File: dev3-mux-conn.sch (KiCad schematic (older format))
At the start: 9 parts, among them J27 Device 3, U16 TS12A44514, U17 TS12A44514, U20 MAX4533, U57 74LS32, U58 LTC1391, U59 LTC1391, U60 LTC1391

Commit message: Updating power + libraries
- Reannotated all parts
- Migrated to new OR gate library
- Reorganized power sheet
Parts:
- removed U57: 74LS32, SMD_Packages:SSOP-14, symbol 74LS32
- added U14: 74LS32, symbol 74LS32
- renumbered C245 to C53, J27 to J29, U20 to U11, U58 to U39, U59 to U40, U60 to U41, U17 to U7, U16 to U7
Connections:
- wire segments 76 -> 77
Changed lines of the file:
@@
-EESchema Schematic File Version 2
+EESchema Schematic File Version 3
 LIBS:SW-Texas
 LIBS:power
@@
 $Descr USLetter 11000 8500
 encoding utf-8
-Sheet 7 15
+Sheet 8 15
 Title ""
 Date ""
@@
 $EndDescr
 $Comp
-L Conn_01x07 J27
+L Conn_01x07 J29
 U 1 1 58EAAC27
 P 850 1200
-F 0 "J27" H 850 1650 50  0000 C CNN
+F 0 "J29" H 850 1650 50  0000 C CNN
 F 1 "Device 3" V 950 1200 50  0000 C CNN
 F 2 "Pin_Headers:Pin_Header_Straight_1x07_Pitch2.54mm" H 850 1200 50  0001 C CNN
@@
 AR Path="/58DEDA38/58EAAC33" Ref="U?"  Part="1"
 AR Path="/58DEDA38/58E9E25B/58EAAC33" Ref="U?"  Part="1"
-AR Path="/58DEDA38/58E9E9F4/58EAAC33" Ref="U17"  Part="4"
-F 0 "U17" H 2650 1450 60  0000 C CNN
+AR Path="/58DEDA38/58E9E9F4/58EAAC33" Ref="U7"  Part="4"
+F 0 "U7" H 2650 1450 60  0000 C CNN
 F 1 "TS12A44514" H 3300 1400 60  0000 C CNN
 F 2 "Housings_SSOP:TSSOP-14_4.4x5mm_Pitch0.65mm" H 3400 2500 60  0001 C CNN
@@
 $Comp
 L TS12A44514 U?
-U 4 1 58EAAC3F
+U 3 1 58EAAC3F
 P 1650 1500
 AR Path="/58DEDA38/58EAAC3F" Ref="U?"  Part="1"
 AR Path="/58DEDA38/58E9E25B/58EAAC3F" Ref="U?"  Part="1"
-AR Path="/58DEDA38/58E9E9F4/58EAAC3F" Ref="U16"  Part="4"
-F 0 "U16" H 1350 1450 60  0000 C CNN
+AR Path="/58DEDA38/58E9E9F4/58EAAC3F" Ref="U7"  Part="3"
+F 0 "U7" H 1350 1450 60  0000 C CNN
 F 1 "TS12A44514" H 1350 1350 60  0000 C CNN
 F 2 "Housings_SSOP:TSSOP-14_4.4x5mm_Pitch0.65mm" H 2150 2800 60  0001 C CNN
@@
 F 7 "TSSOP14" H 1950 2700 60  0001 C CNN "Package ID"
 F 8 "0.00@0" H 1700 2500 60  0001 C CNN "Pricing"
-	4    1650 1500
-	1    0    0    -1
-$EndComp
-$Comp
-L C_Small C245
+	3    1650 1500
+	1    0    0    -1
+$EndComp
+$Comp
+L C_Small C53
 U 1 1 58EAAC46
 P 2450 1200
-F 0 "C245" H 2460 1270 50  0000 L CNN
+F 0 "C53" H 2460 1270 50  0000 L CNN
 F 1 "10u" H 2460 1120 50  0000 L CNN
 F 2 "Capacitors_SMD:C_0603" H 2450 1200 50  0001 C CNN
@@
 AUDIO-GROUND
 $Comp
-L LTC1391 U58
+L LTC1391 U39
 U 1 1 58EAAC56
 P 6350 1450
-F 0 "U58" H 6100 1950 60  0000 C CNN
+F 0 "U39" H 6100 1950 60  0000 C CNN
 F 1 "LTC1391" H 6700 1900 60  0000 C CNN
 F 2 "Housings_SSOP:SSOP-16_3.9x4.9mm_Pitch0.635mm" H 6450 2700 60  0001 C CNN
@@
 DOUT
 $Comp
-L +5VD #PWR0211
+L +5VD #PWR078
 U 1 1 58EAAC61
 P 6350 750
-F 0 "#PWR0211" H 6350 600 50  0001 C CNN
+F 0 "#PWR078" H 6350 600 50  0001 C CNN
 F 1 "+5VD" H 6350 890 50  0000 C CNN
 F 2 "" H 6350 750 50  0001 C CNN
@@
 $EndComp
 $Comp
-L GNDREF #PWR0212
+L GNDREF #PWR079
 U 1 1 58EAAC67
 P 6350 2050
-F 0 "#PWR0212" H 6350 1800 50  0001 C CNN
+F 0 "#PWR079" H 6350 1800 50  0001 C CNN
 F 1 "GNDREF" H 6350 1900 50  0000 C CNN
 F 2 "" H 6350 2050 50  0001 C CNN
@@
 Text HLabel 7100 1800 2    60   Input ~ 0
 MIC-IN-7
-$Comp
-L 74LS32 U57
-U 1 1 58EAAC75
-P 3450 2900
-F 0 "U57" H 3450 2950 50  0000 C CNN
-F 1 "74LS32" H 3450 2850 50  0000 C CNN
-F 2 "SMD_Packages:SSOP-14" H 3450 2900 50  0001 C CNN
-F 3 "" H 3450 2900 50  0001 C CNN
-F 4 "0.00@0" H 3450 2900 60  0001 C CNN "Pricing"
-	1    3450 2900
-	-1   0    0    1
-$EndComp
-$Comp
-L 74LS32 U57
-U 2 1 58EAAC7C
-P 3450 4600
-F 0 "U57" H 3450 4650 50  0000 C CNN
-F 1 "74LS32" H 3450 4550 50  0000 C CNN
-F 2 "SMD_Packages:SSOP-14" H 3450 4600 50  0001 C CNN
-F 3 "" H 3450 4600 50  0001 C CNN
-F 4 "0.00@0" H 3450 4600 60  0001 C CNN "Pricing"
-	2    3450 4600
-	-1   0    0    1
-$EndComp
 Text HLabel 4250 2800 2    60   Input ~ 0
 MIC-MUTE-Pi
@@
 P 2300 1650
 AR Path="/58DEDA38/58E9E25B/58EAAC89" Ref="U?"  Part="1"
-AR Path="/58DEDA38/58E9E9F4/58EAAC89" Ref="U20"  Part="4"
-F 0 "U20" H 2400 1850 60  0000 C CNN
+AR Path="/58DEDA38/58E9E9F4/58EAAC89" Ref="U11"  Part="4"
+F 0 "U11" H 2400 1850 60  0000 C CNN
 F 1 "MAX4533" H 1950 1400 60  0000 C CNN
 F 2 "Housings_SSOP:SSOP-20_4.4x6.5mm_Pitch0.65mm" H 2400 2600 60  0001 C CNN
@@
 PTT-7
 $Comp
-L LTC1391 U59
+L LTC1391 U40
 U 1 1 58EAACA4
 P 6350 3250
-F 0 "U59" H 6100 3750 60  0000 C CNN
+F 0 "U40" H 6100 3750 60  0000 C CNN
 F 1 "LTC1391" H 6700 3700 60  0000 C CNN
 F 2 "Housings_SSOP:SSOP-16_3.9x4.9mm_Pitch0.635mm" H 6450 4500 60  0001 C CNN
@@
 $EndComp
 $Comp
-L +5VD #PWR0213
+L +5VD #PWR080
 U 1 1 58EAACAB
 P 6350 2550
-F 0 "#PWR0213" H 6350 2400 50  0001 C CNN
+F 0 "#PWR080" H 6350 2400 50  0001 C CNN
 F 1 "+5VD" H 6350 2690 50  0000 C CNN
 F 2 "" H 6350 2550 50  0001 C CNN
@@
 $EndComp
 $Comp
-L GNDREF #PWR0214
+L GNDREF #PWR081
 U 1 1 58EAACB1
 P 6350 3850
-F 0 "#PWR0214" H 6350 3600 50  0001 C CNN
+F 0 "#PWR081" H 6350 3600 50  0001 C CNN
 F 1 "GNDREF" H 6350 3700 50  0000 C CNN
 F 2 "" H 6350 3850 50  0001 C CNN
@@
 $EndComp
 $Comp
-L LTC1391 U60
+L LTC1391 U41
 U 1 1 58EAACBB
 P 6350 4950
-F 0 "U60" H 6100 5450 60  0000 C CNN
+F 0 "U41" H 6100 5450 60  0000 C CNN
 F 1 "LTC1391" H 6700 5400 60  0000 C CNN
 F 2 "Housings_SSOP:SSOP-16_3.9x4.9mm_Pitch0.635mm" H 6450 6200 60  0001 C CNN
@@
 $EndComp
 $Comp
-L +5VD #PWR0215
+L +5VD #PWR082
 U 1 1 58EAACC2
 P 6350 4250
-F 0 "#PWR0215" H 6350 4100 50  0001 C CNN
+F 0 "#PWR082" H 6350 4100 50  0001 C CNN
 F 1 "+5VD" H 6350 4390 50  0000 C CNN
 F 2 "" H 6350 4250 50  0001 C CNN
@@
 $EndComp
 $Comp
-L GNDREF #PWR0216
+L GNDREF #PWR083
 U 1 1 58EAACC8
 P 6350 5550
-F 0 "#PWR0216" H 6350 5300 50  0001 C CNN
+F 0 "#PWR083" H 6350 5300 50  0001 C CNN
 F 1 "GNDREF" H 6350 5400 50  0000 C CNN
 F 2 "" H 6350 5550 50  0001 C CNN
@@
 Connection ~ 3300 1550
 Wire Wire Line
-	2850 4600 2650 4600
+	2650 4600 3450 4600
 Wire Wire Line
 	2650 4600 2650 1750
@@
 Text Notes 1450 3000 0    60   ~ 0
 1-Audio Ground\n2-L audio to MUX\n3-R audio to MUX\n4-Mic +\n5-Mic -\n6- PTT +\n7- PTT -
+$Comp
+L 74LS32 U?
+U 3 1 59D24359
+P 3750 2900
+AR Path="/58DEDA38/58E9E2BE/59D24359" Ref="U?"  Part="1"
+AR Path="/58DEDA38/58E9E9F4/59D24359" Ref="U14"  Part="3"
+F 0 "U14" H 3750 2583 50  0000 C CNN
+F 1 "74LS32" H 3750 2674 50  0000 C CNN
+F 2 "" H 3750 2900 50  0001 C CNN
+F 3 "" H 3750 2900 50  0001 C CNN
+	3    3750 2900
+	-1   0    0    1
+$EndComp
+Wire Wire Line
+	2850 2900 3450 2900
+$Comp
+L 74LS32 U?
+U 4 1 59D24361
+P 3750 4600
+AR Path="/58DEDA38/58E9E2BE/59D24361" Ref="U?"  Part="2"
+AR Path="/58DEDA38/58E9E9F4/59D24361" Ref="U14"  Part="4"
+F 0 "U14" H 3750 4283 50  0000 C CNN
+F 1 "74LS32" H 3750 4374 50  0000 C CNN
+F 2 "" H 3750 4600 50  0001 C CNN
+F 3 "" H 3750 4600 50  0001 C CNN
+	4    3750 4600
+	-1   0    0    1
+$EndComp
 $EndSCHEMATC

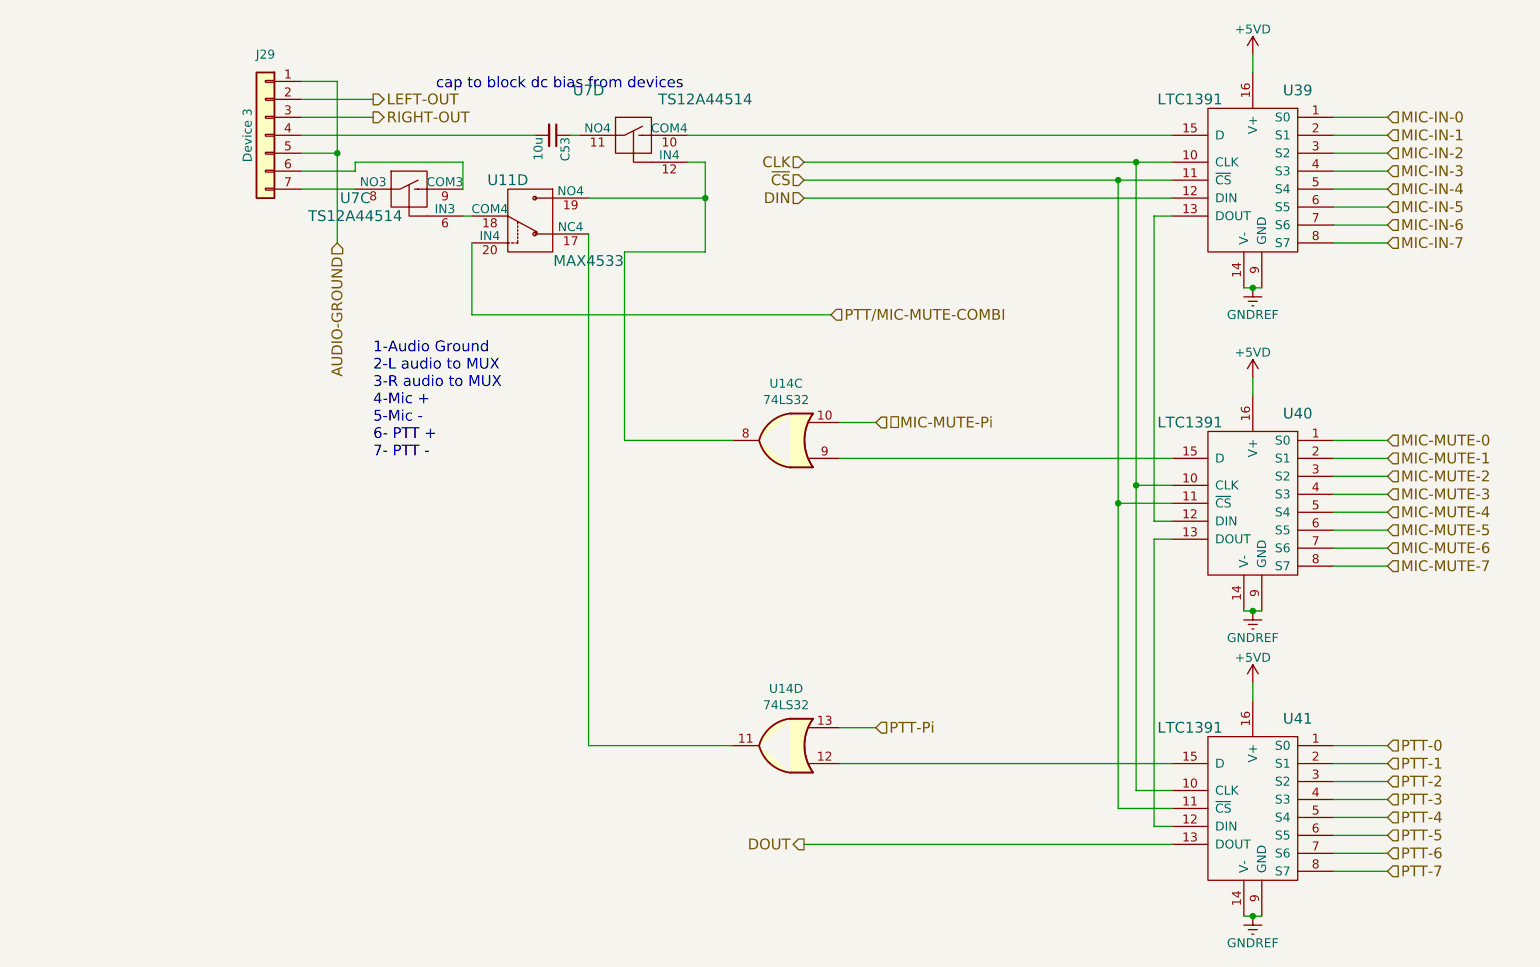
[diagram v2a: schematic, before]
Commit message: Updates during pcb layout
Added more net labels
moved switches and OR gates to +5V instead of +5VD
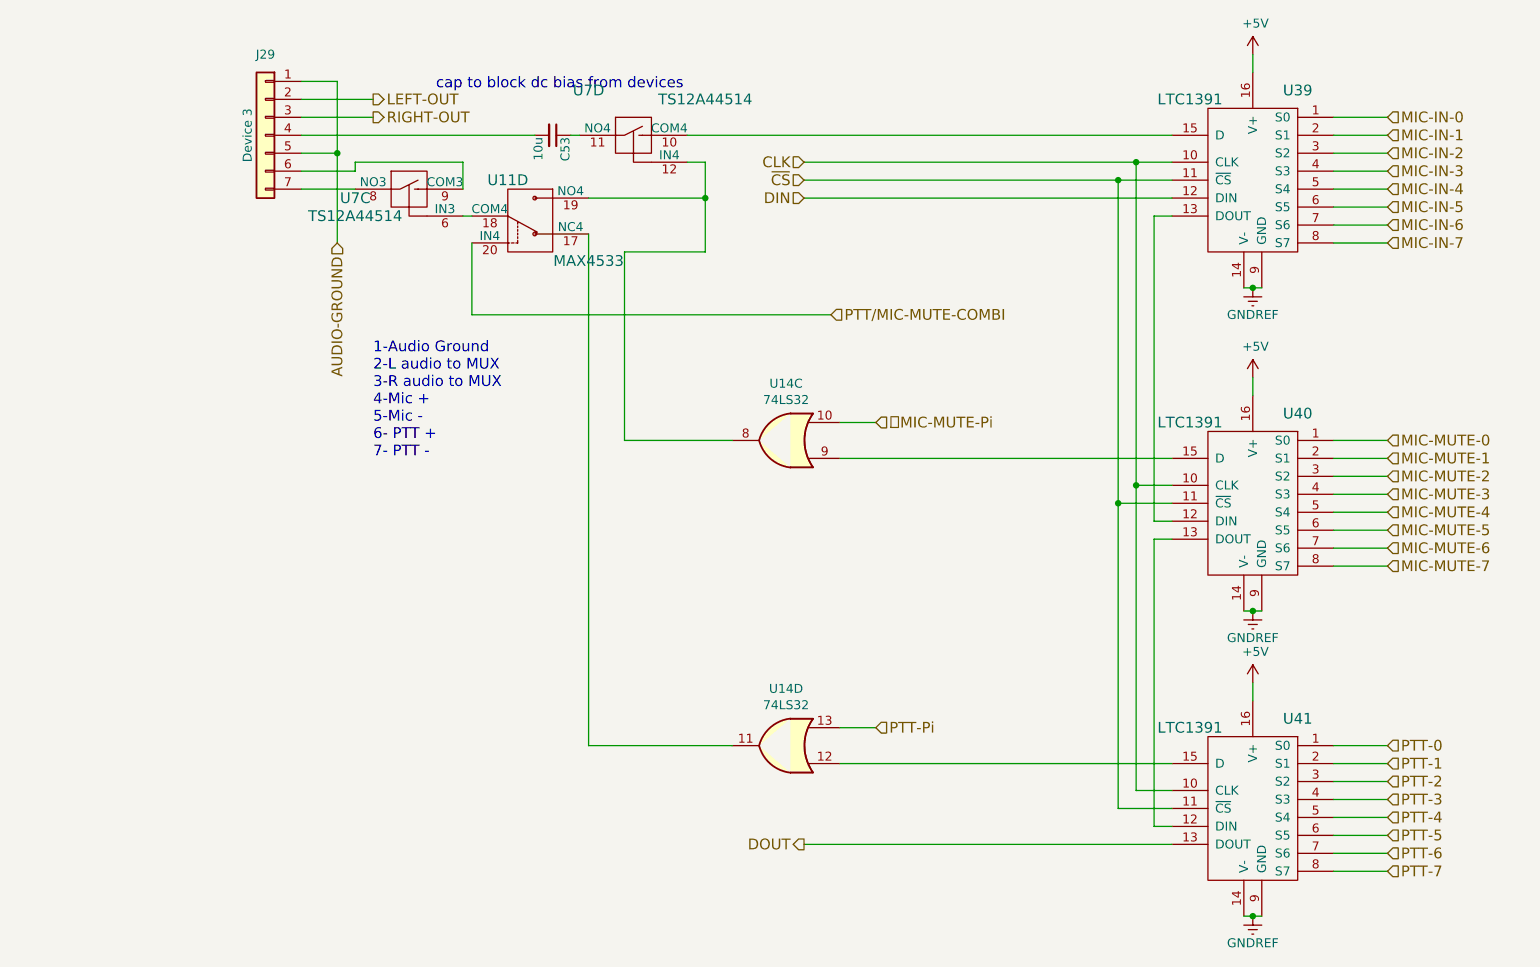
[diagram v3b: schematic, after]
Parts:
- J29: footprint Pin_Headers:Pin_Header_Straight_1x07_Pitch2.54mm -> SW-TEConn:3-794681-8
- U14: footprint (none) -> Housings_SSOP:SSOP-14_5.3x6.2mm_Pitch0.65mm
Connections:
- net +5VD renamed +5V
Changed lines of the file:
@@
 LIBS:SW-Diodes-Inc
 LIBS:interface
+LIBS:SW-gElectroMech
 LIBS:edc-mux-board-cache
 EELAYER 26 0
@@
 F 0 "J29" H 850 1650 50  0000 C CNN
 F 1 "Device 3" V 950 1200 50  0000 C CNN
-F 2 "Pin_Headers:Pin_Header_Straight_1x07_Pitch2.54mm" H 850 1200 50  0001 C CNN
+F 2 "SW-TEConn:3-794681-8" H 850 1200 50  0001 C CNN
 F 3 "" H 850 1200 50  0001 C CNN
 F 4 "0.00@0" H 850 1200 60  0001 C CNN "Pricing"
@@
 Text HLabel 3850 5150 0    60   Output ~ 0
 DOUT
-$Comp
-L +5VD #PWR078
-U 1 1 58EAAC61
-P 6350 750
-F 0 "#PWR078" H 6350 600 50  0001 C CNN
-F 1 "+5VD" H 6350 890 50  0000 C CNN
-F 2 "" H 6350 750 50  0001 C CNN
-F 3 "" H 6350 750 50  0001 C CNN
-	1    6350 750
-	1    0    0    -1
-$EndComp
 $Comp
 L GNDREF #PWR079
@@
 $EndComp
 $Comp
-L +5VD #PWR080
-U 1 1 58EAACAB
-P 6350 2550
-F 0 "#PWR080" H 6350 2400 50  0001 C CNN
-F 1 "+5VD" H 6350 2690 50  0000 C CNN
-F 2 "" H 6350 2550 50  0001 C CNN
-F 3 "" H 6350 2550 50  0001 C CNN
-	1    6350 2550
-	1    0    0    -1
-$EndComp
-$Comp
 L GNDREF #PWR081
 U 1 1 58EAACB1
@@
 $EndComp
 $Comp
-L +5VD #PWR082
-U 1 1 58EAACC2
-P 6350 4250
-F 0 "#PWR082" H 6350 4100 50  0001 C CNN
-F 1 "+5VD" H 6350 4390 50  0000 C CNN
-F 2 "" H 6350 4250 50  0001 C CNN
-F 3 "" H 6350 4250 50  0001 C CNN
-	1    6350 4250
-	1    0    0    -1
-$EndComp
-$Comp
 L GNDREF #PWR083
 U 1 1 58EAACC8
@@
 $EndComp
 Wire Wire Line
-	1250 900  1250 1800
+	1250 900  1250 1300
+Wire Wire Line
+	1250 1300 1250 1800
 Wire Wire Line
 	1050 900  1250 900
@@
 	3850 1550 5900 1550
 Wire Wire Line
-	3850 1450 5900 1450
-Wire Wire Line
-	3850 1350 5900 1350
+	3850 1450 5600 1450
+Wire Wire Line
+	5600 1450 5900 1450
+Wire Wire Line
+	3850 1350 5700 1350
+Wire Wire Line
+	5700 1350 5900 1350
 Wire Wire Line
 	6350 750  6350 850
 Wire Wire Line
-	6300 2050 6400 2050
+	6300 2050 6350 2050
+Wire Wire Line
+	6350 2050 6400 2050
 Wire Wire Line
 	6350 2050 6350 2050
 Connection ~ 6350 2050
 Wire Wire Line
-	3300 1350 3300 1850
+	3300 1350 3300 1550
+Wire Wire Line
+	3300 1550 3300 1850
 Wire Wire Line
 	3300 1850 2850 1850
@@
 	6350 2550 6350 2650
 Wire Wire Line
-	6300 3850 6400 3850
+	6300 3850 6350 3850
+Wire Wire Line
+	6350 3850 6400 3850
 Wire Wire Line
 	6350 3850 6350 3850
@@
 	6350 4250 6350 4350
 Wire Wire Line
-	6300 5550 6400 5550
+	6300 5550 6350 5550
+Wire Wire Line
+	6350 5550 6400 5550
 Wire Wire Line
 	6350 5550 6350 5550
 Connection ~ 6350 5550
 Wire Wire Line
-	5700 1350 5700 4850
+	5700 1350 5700 3150
+Wire Wire Line
+	5700 3150 5700 4850
 Connection ~ 5700 3150
 Connection ~ 5700 1350
 Wire Wire Line
-	5600 1450 5600 4950
+	5600 1450 5600 3250
+Wire Wire Line
+	5600 3250 5600 4950
 Connection ~ 5600 3250
 Connection ~ 5600 1450
@@
 F 0 "U14" H 3750 2583 50  0000 C CNN
 F 1 "74LS32" H 3750 2674 50  0000 C CNN
-F 2 "" H 3750 2900 50  0001 C CNN
+F 2 "Housings_SSOP:SSOP-14_5.3x6.2mm_Pitch0.65mm" H 3750 2900 50  0001 C CNN
 F 3 "" H 3750 2900 50  0001 C CNN
 	3    3750 2900
@@
 F 0 "U14" H 3750 4283 50  0000 C CNN
 F 1 "74LS32" H 3750 4374 50  0000 C CNN
-F 2 "" H 3750 4600 50  0001 C CNN
+F 2 "Housings_SSOP:SSOP-14_5.3x6.2mm_Pitch0.65mm" H 3750 4600 50  0001 C CNN
 F 3 "" H 3750 4600 50  0001 C CNN
 	4    3750 4600
 	-1   0    0    1
 $EndComp
+$Comp
+L +5V #PWR?
+U 1 1 59D27246
+P 6350 750
+F 0 "#PWR?" H 6350 600 50  0001 C CNN
+F 1 "+5V" H 6365 923 50  0000 C CNN
+F 2 "" H 6350 750 50  0001 C CNN
+F 3 "" H 6350 750 50  0001 C CNN
+	1    6350 750
+	1    0    0    -1
+$EndComp
+$Comp
+L +5V #PWR?
+U 1 1 59D27320
+P 6350 2550
+F 0 "#PWR?" H 6350 2400 50  0001 C CNN
+F 1 "+5V" H 6365 2723 50  0000 C CNN
+F 2 "" H 6350 2550 50  0001 C CNN
+F 3 "" H 6350 2550 50  0001 C CNN
+	1    6350 2550
+	1    0    0    -1
+$EndComp
+$Comp
+L +5V #PWR?
+U 1 1 59D273AE
+P 6350 4250
+F 0 "#PWR?" H 6350 4100 50  0001 C CNN
+F 1 "+5V" H 6365 4423 50  0000 C CNN
+F 2 "" H 6350 4250 50  0001 C CNN
+F 3 "" H 6350 4250 50  0001 C CNN
+	1    6350 4250
+	1    0    0    -1
+$EndComp
 $EndSCHEMATC

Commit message: Lots of progress on PCB
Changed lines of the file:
@@
 $EndComp
 Wire Wire Line
-	1250 900  1250 1300
-Wire Wire Line
-	1250 1300 1250 1800
+	1250 900  1250 1800
 Wire Wire Line
 	1050 900  1250 900
@@
 	3850 1550 5900 1550
 Wire Wire Line
-	3850 1450 5600 1450
-Wire Wire Line
-	5600 1450 5900 1450
-Wire Wire Line
-	3850 1350 5700 1350
-Wire Wire Line
-	5700 1350 5900 1350
+	3850 1450 5900 1450
+Wire Wire Line
+	3850 1350 5900 1350
 Wire Wire Line
 	6350 750  6350 850
 Wire Wire Line
-	6300 2050 6350 2050
-Wire Wire Line
-	6350 2050 6400 2050
+	6300 2050 6400 2050
 Wire Wire Line
 	6350 2050 6350 2050
 Connection ~ 6350 2050
 Wire Wire Line
-	3300 1350 3300 1550
-Wire Wire Line
-	3300 1550 3300 1850
+	3300 1350 3300 1850
 Wire Wire Line
 	3300 1850 2850 1850
@@
 	6350 2550 6350 2650
 Wire Wire Line
-	6300 3850 6350 3850
-Wire Wire Line
-	6350 3850 6400 3850
+	6300 3850 6400 3850
 Wire Wire Line
 	6350 3850 6350 3850
@@
 	6350 4250 6350 4350
 Wire Wire Line
-	6300 5550 6350 5550
-Wire Wire Line
-	6350 5550 6400 5550
+	6300 5550 6400 5550
 Wire Wire Line
 	6350 5550 6350 5550
 Connection ~ 6350 5550
 Wire Wire Line
-	5700 1350 5700 3150
-Wire Wire Line
-	5700 3150 5700 4850
+	5700 1350 5700 4850
 Connection ~ 5700 3150
 Connection ~ 5700 1350
 Wire Wire Line
-	5600 1450 5600 3250
-Wire Wire Line
-	5600 3250 5600 4950
+	5600 1450 5600 4950
 Connection ~ 5600 3250
 Connection ~ 5600 1450
@@
 $EndComp
 $Comp
-L +5V #PWR?
+L +5V #PWR078
 U 1 1 59D27246
 P 6350 750
-F 0 "#PWR?" H 6350 600 50  0001 C CNN
+F 0 "#PWR078" H 6350 600 50  0001 C CNN
 F 1 "+5V" H 6365 923 50  0000 C CNN
 F 2 "" H 6350 750 50  0001 C CNN
@@
 $EndComp
 $Comp
-L +5V #PWR?
+L +5V #PWR080
 U 1 1 59D27320
 P 6350 2550
-F 0 "#PWR?" H 6350 2400 50  0001 C CNN
+F 0 "#PWR080" H 6350 2400 50  0001 C CNN
 F 1 "+5V" H 6365 2723 50  0000 C CNN
 F 2 "" H 6350 2550 50  0001 C CNN
@@
 $EndComp
 $Comp
-L +5V #PWR?
+L +5V #PWR082
 U 1 1 59D273AE
 P 6350 4250
-F 0 "#PWR?" H 6350 4100 50  0001 C CNN
+F 0 "#PWR082" H 6350 4100 50  0001 C CNN
 F 1 "+5V" H 6365 4423 50  0000 C CNN
 F 2 "" H 6350 4250 50  0001 C CNN
